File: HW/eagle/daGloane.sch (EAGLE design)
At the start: 64 parts, among them IC1 STM32F103CBT6, IC2 MCP1252-33X50

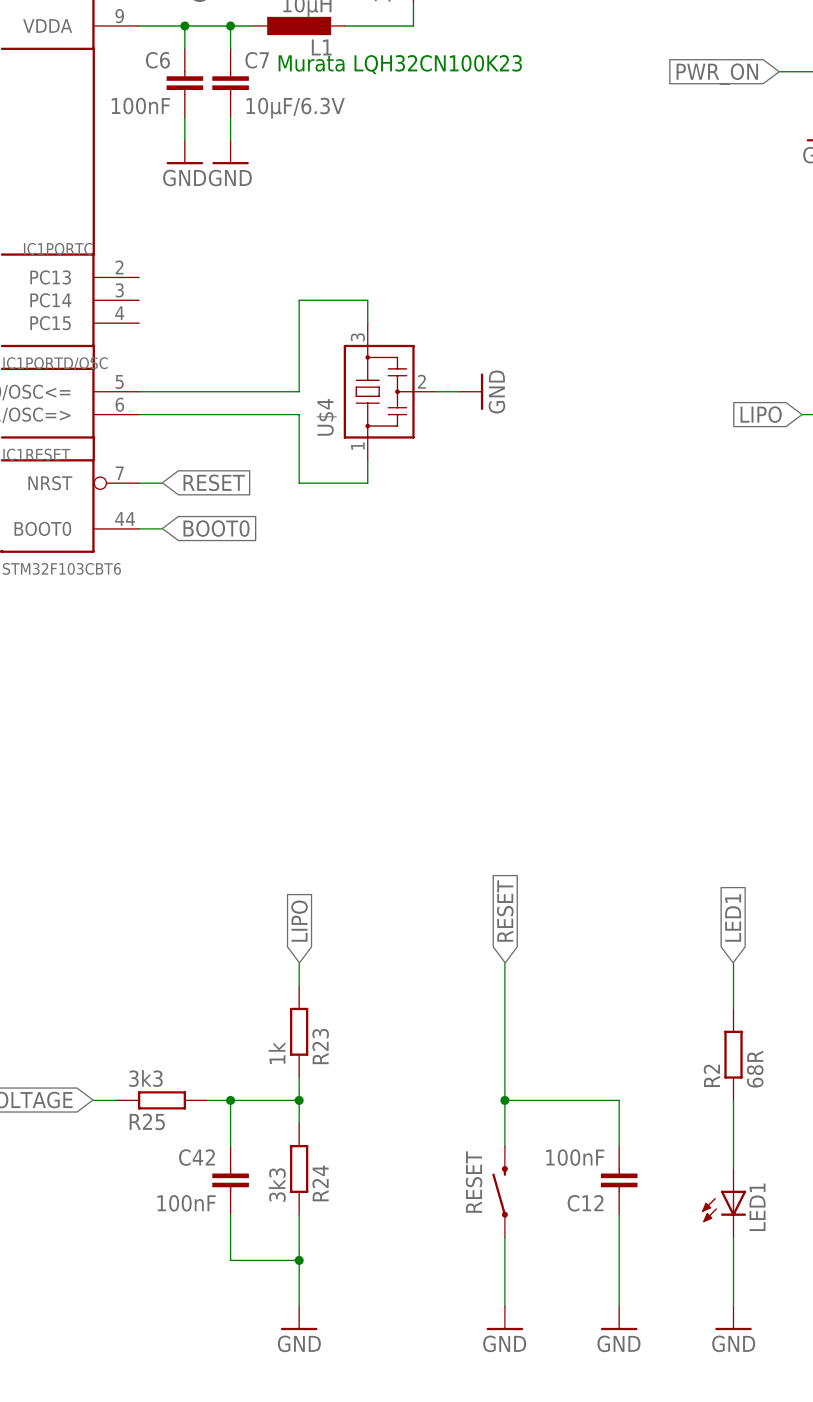
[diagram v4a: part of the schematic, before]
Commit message: reset buttom removed.
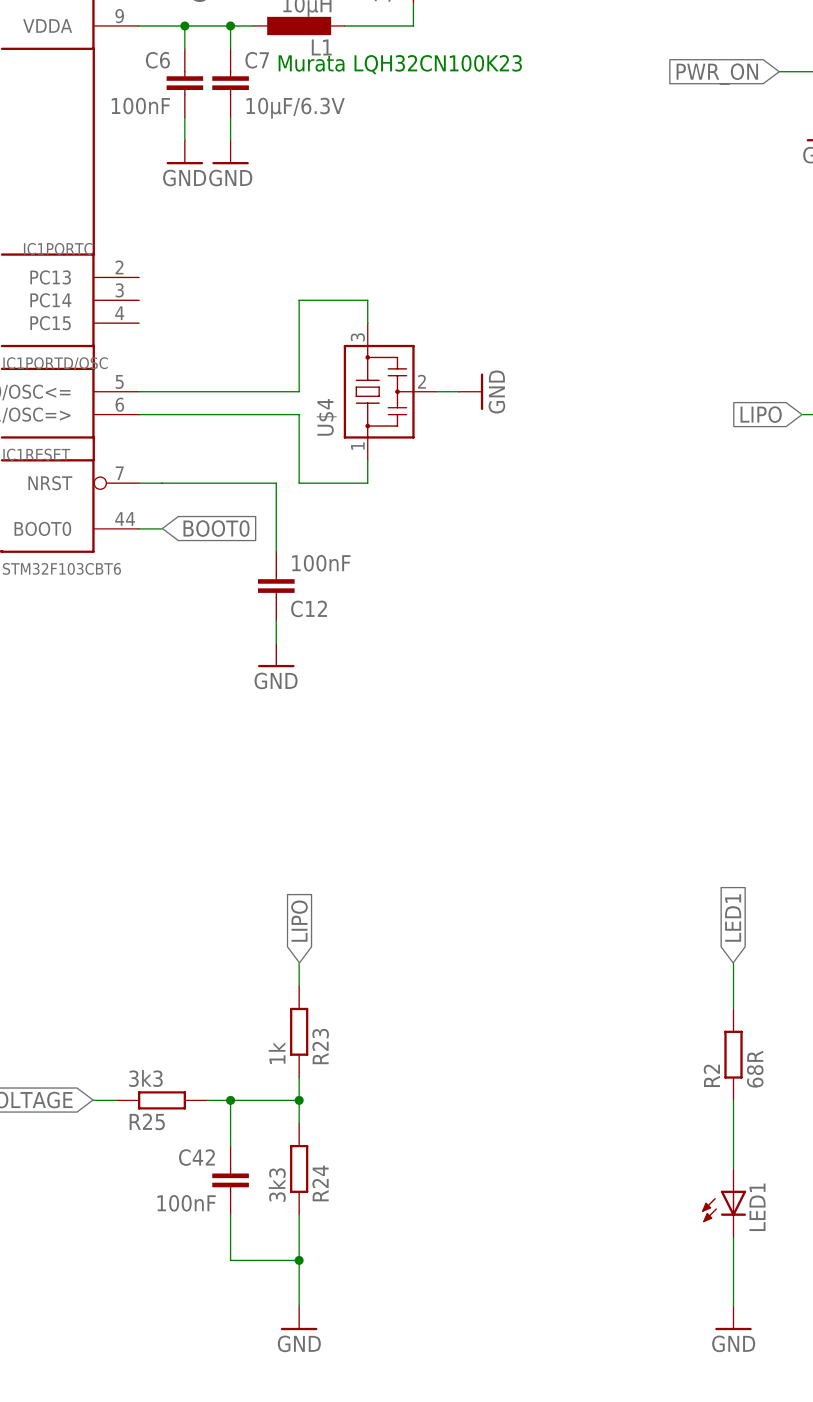
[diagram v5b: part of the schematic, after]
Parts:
- removed RESET: SWITCH-MOMENTARY-2SMD, SparkFun:SWITCH-MOMENTARY-2SMD
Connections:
- net GND: no longer RESET.1
- net RESET: no longer RESET.2
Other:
- moved on the sheet: C12
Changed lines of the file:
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@@
 <part name="C12" library="rcl" deviceset="C-EU" device="C0603" value="100nF"/>
 <part name="GND6" library="supply1" deviceset="GND" device=""/>
-<part name="GND64" library="supply1" deviceset="GND" device=""/>
 <part name="R1" library="rcl" deviceset="R-EU_" device="R0603" value="10k"/>
 <part name="GND12" library="supply1" deviceset="GND" device=""/>
@@
 <part name="C42" library="rcl" deviceset="C-EU" device="C0603" value="100nF"/>
 <part name="R2" library="rcl" deviceset="R-EU_" device="R0603" value="68R"/>
-<part name="RESET" library="SparkFun" deviceset="SWITCH-MOMENTARY-2" device="SMD"/>
 <part name="BOOTMD" library="SparkFun" deviceset="JUMPER-2" device="PTH"/>
 <part name="GND41" library="supply1" deviceset="GND" device=""/>
@@
 <instance part="C2" gate="G$1" x="121.92" y="220.98" rot="R90"/>
 <instance part="R6" gate="G$1" x="185.42" y="48.26" rot="R90"/>
-<instance part="C12" gate="G$1" x="160.02" y="33.02" rot="R180"/>
-<instance part="GND6" gate="1" x="160.02" y="17.78"/>
-<instance part="GND64" gate="1" x="147.32" y="17.78"/>
+<instance part="C12" gate="G$1" x="121.92" y="99.06" rot="MR180"/>
+<instance part="GND6" gate="1" x="121.92" y="91.44"/>
 <instance part="R1" gate="G$1" x="73.66" y="33.02" rot="R90"/>
 <instance part="GND12" gate="1" x="73.66" y="17.78"/>
@@
 <instance part="C7" gate="G$1" x="116.84" y="157.48"/>
 <instance part="GND26" gate="1" x="111.76" y="147.32"/>
-<instance part="GND27" gate="1" x="116.84" y="147.32"/>
+<instance part="GND27" gate="1" x="116.84" y="147.32" rot="MR0"/>
 <instance part="GND9" gate="1" x="243.84" y="66.04" rot="R90"/>
 <instance part="C1" gate="G$1" x="121.92" y="233.68" rot="R90"/>
@@
 <instance part="C42" gate="G$1" x="116.84" y="35.56" rot="MR0"/>
 <instance part="R2" gate="G$1" x="172.72" y="48.26" rot="R90"/>
-<instance part="RESET" gate="G$1" x="147.32" y="33.02" smashed="yes" rot="R90">
-<attribute name="NAME" x="144.78" y="30.48" size="1.778" layer="95" rot="R90"/>
-</instance>
 <instance part="BOOTMD" gate="A" x="78.74" y="53.34" rot="R270"/>
 <instance part="GND41" gate="1" x="185.42" y="17.78" rot="MR0"/>
@@
 <net name="GND" class="0">
 <segment>
-<wire x1="160.02" y1="20.32" x2="160.02" y2="30.48" width="0.1524" layer="91"/>
 <pinref part="GND6" gate="1" pin="GND"/>
 <pinref part="C12" gate="G$1" pin="1"/>
+<wire x1="121.92" y1="93.98" x2="121.92" y2="96.52" width="0.1524" layer="91"/>
 </segment>
 <segment>
@@
 <pinref part="GND46" gate="1" pin="GND"/>
 <pinref part="C42" gate="G$1" pin="2"/>
-</segment>
-<segment>
-<wire x1="147.32" y1="27.94" x2="147.32" y2="20.32" width="0.1524" layer="91"/>
-<pinref part="RESET" gate="G$1" pin="1"/>
-<pinref part="GND64" gate="1" pin="GND"/>
 </segment>
 <segment>
@@
 <segment>
 <wire x1="109.22" y1="111.76" x2="106.68" y2="111.76" width="0.1524" layer="91"/>
-<label x="109.26" y="111.8" size="1.778" layer="95" xref="yes"/>
 <pinref part="IC1" gate="RESET" pin="NRST"/>
-</segment>
-<segment>
-<wire x1="147.32" y1="43.18" x2="147.32" y2="38.1" width="0.1524" layer="91"/>
-<wire x1="147.32" y1="43.18" x2="147.32" y2="58.42" width="0.1524" layer="91"/>
-<wire x1="160.02" y1="38.1" x2="160.02" y2="43.18" width="0.1524" layer="91"/>
-<wire x1="160.02" y1="43.18" x2="147.32" y2="43.18" width="0.1524" layer="91"/>
-<junction x="147.32" y="43.18"/>
-<label x="147.36" y="58.46" size="1.778" layer="95" rot="R90" xref="yes"/>
 <pinref part="C12" gate="G$1" pin="2"/>
-<pinref part="RESET" gate="G$1" pin="2"/>
+<wire x1="109.22" y1="111.76" x2="121.92" y2="111.76" width="0.1524" layer="91"/>
+<wire x1="121.92" y1="111.76" x2="121.92" y2="104.14" width="0.1524" layer="91"/>
 </segment>
 </net>

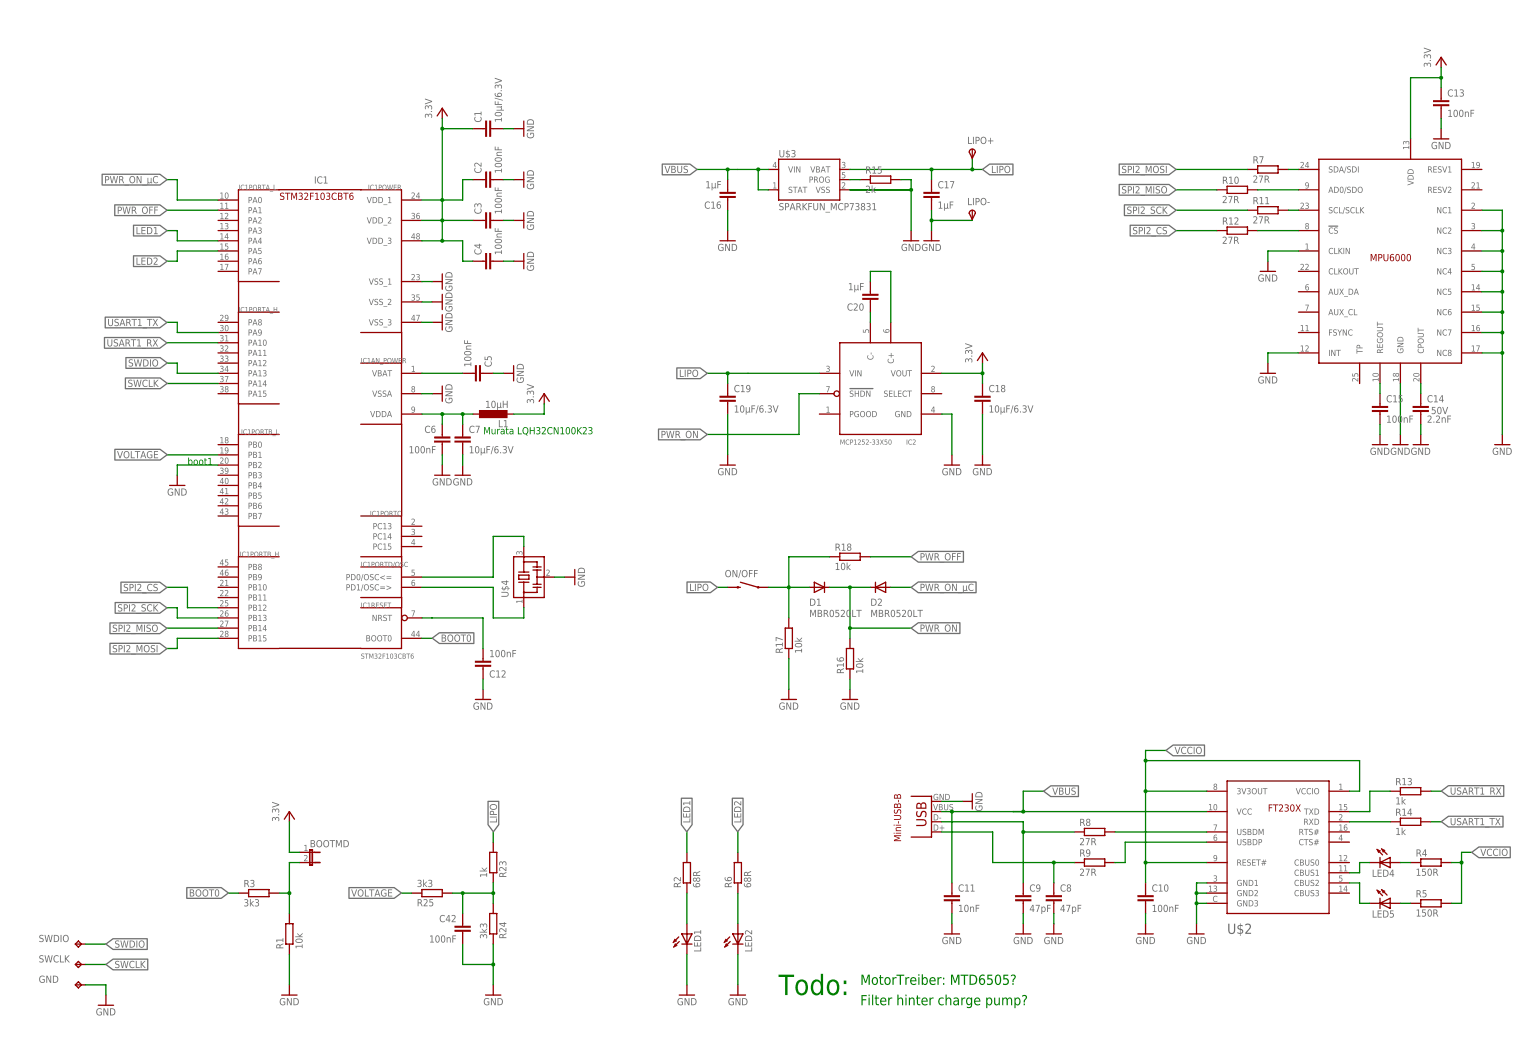
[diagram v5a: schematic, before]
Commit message: STM32 replaced by derivate with a smaller footprint: VFQFPN36
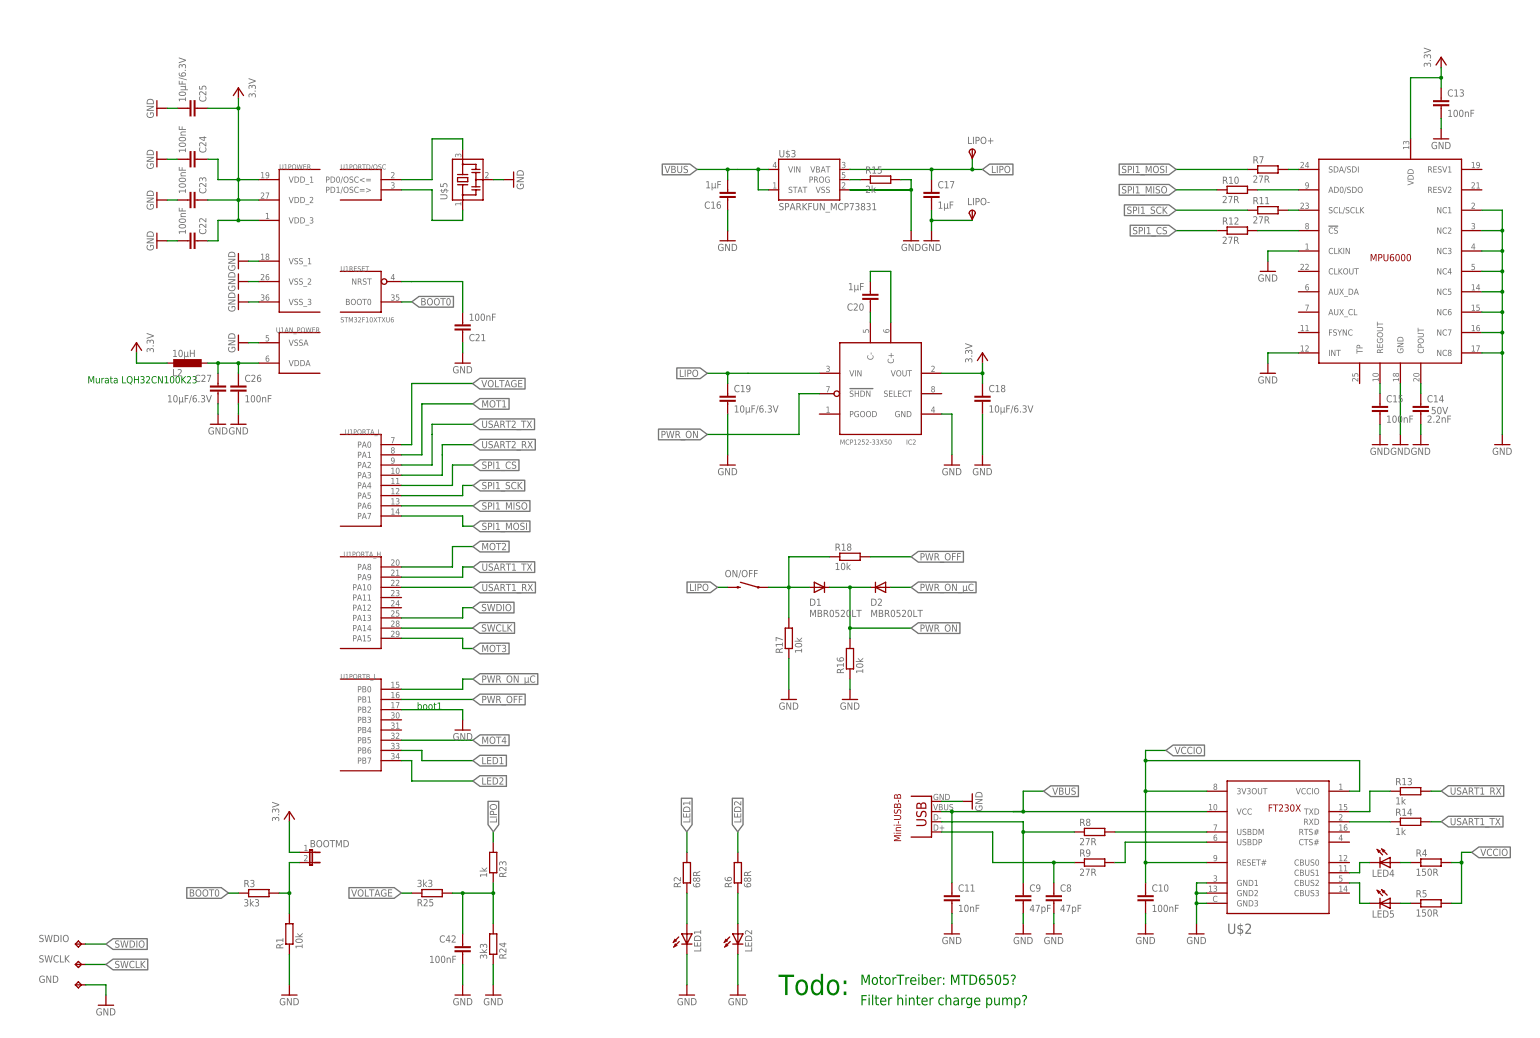
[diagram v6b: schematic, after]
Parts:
- removed C1, C7: 10µF/6.3V, rcl:C-EUC0805
- removed C12, C2, C3, C4, C5, C6: 100nF, rcl:C-EUC0603
- removed IC1: STM32F103CBT6, stm32:STM32F10XCXT6
- removed L1: 10µH, rcl:L-EUL1210
- removed U$4: MURATA-FILTER_CSTCE__G, canBLC2:MURATA-FILTER_CSTCE__G
- added C21, C22, C23, C24, C26: 100nF, rcl:C-EUC0603
- added C25, C27: 10µF/6.3V, rcl:C-EUC0805
- added L2: 10µH, rcl:L-EUL1210
- added U$5: MURATA-FILTER_CSTCE__G, canBLC2:MURATA-FILTER_CSTCE__G
- added U1: STM32F10XTXU6, stm32:STM32F10XTXU6
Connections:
- removed net N$1: IC1PORTD/OSC.PD1/OSC=>, U$4.1
- removed net N$7: IC1PORTD/OSC.PD0/OSC<=, U$4.3
- removed net RESET: C12.2, IC1RESET.NRST
- removed net SPI2_CS: IC1PORTB_H.PB12, R12.1
- removed net SPI2_MISO: IC1PORTB_H.PB14, R10.1
- removed net SPI2_MOSI: IC1PORTB_H.PB15, R7.1
- removed net SPI2_SCK: IC1PORTB_H.PB13, R11.1
- removed net VBAT: C5.2, IC1AN_POWER.VBAT
- removed net VDDA: C6.1, C7.1, IC1AN_POWER.VDDA, L1.1
- new net MOT1: U1PORTA_L.PA1
- new net MOT2: U1PORTA_H.PA8
- new net MOT3: U1PORTA_H.PA15
- new net MOT4: U1PORTB_L.PB5
- new net N$2: U$5.3, U1PORTD/OSC.PD0/OSC<=
- new net N$25: U$5.1, U1PORTD/OSC.PD1/OSC=>
- new net RESET1: C21.2, U1RESET.NRST
- new net SPI1_CS: R12.1, U1PORTA_L.PA4
- new net SPI1_MISO: R10.1, U1PORTA_L.PA6
- new net SPI1_MOSI: R7.1, U1PORTA_L.PA7
- new net SPI1_SCK: R11.1, U1PORTA_L.PA5
- new net USART2_RX: U1PORTA_L.PA3
- new net USART2_TX: U1PORTA_L.PA2
- new net VDDA1: C26.1, C27.1, L2.1
- net BOOT0: now also U1RESET.BOOT0; no longer IC1RESET.BOOT0
- net GND: now also C21.1, C22.2, C23.2, C24.2, C25.2, C26.2, C27.2, U$5.2, U1PORTB_L.PB2; no longer C1.2, C12.1, C2.2, C3.2, C4.2, C5.1, C6.2, C7.2, IC1AN_POWER.VSSA, IC1PORTB_L.PB2, IC1POWER.VSS_1, IC1POWER.VSS_2, IC1POWER.VSS_3, U$4.2
- net LED1: now also U1PORTB_L.PB6; no longer IC1PORTA_L.PA4
- net LED2: now also U1PORTB_L.PB7; no longer IC1PORTA_L.PA5
- net PWR_OFF: now also U1PORTB_L.PB1; no longer IC1PORTA_L.PA1
- net PWR_ON_µC: now also U1PORTB_L.PB0; no longer IC1PORTA_L.PA0
- net SWCLK: now also U1PORTA_H.PA14; no longer IC1PORTA_H.PA14
- net SWDIO: now also U1PORTA_H.PA13; no longer IC1PORTA_H.PA13
- net USART1_RX: now also U1PORTA_H.PA10; no longer IC1PORTA_H.PA10
- net USART1_TX: now also U1PORTA_H.PA9; no longer IC1PORTA_H.PA9
- net VCC: now also C22.1, C23.1, C24.1, C25.1, L2.2, U1POWER.VDD_1, U1POWER.VDD_2, U1POWER.VDD_3; no longer C1.1, C2.1, C3.1, C4.1, IC1POWER.VDD_1, IC1POWER.VDD_2, IC1POWER.VDD_3, L1.2
- net VOLTAGE: now also U1PORTA_L.PA0; no longer IC1PORTB_L.PB1
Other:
- note removed: "IC1"
- note removed: "STM32F103CBT6"
- moved on the sheet: C42, R24
